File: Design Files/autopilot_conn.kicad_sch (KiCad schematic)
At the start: 7 parts, among them J10 Conn_01x06_MountingPin, J12 Conn_01x02_MountingPin, J13 Conn_01x02_MountingPin, J3 Conn_01x04_MountingPin, J4 Conn_01x06_MountingPin, J6 Conn_01x04_MountingPin, J9 Conn_01x04_MountingPin

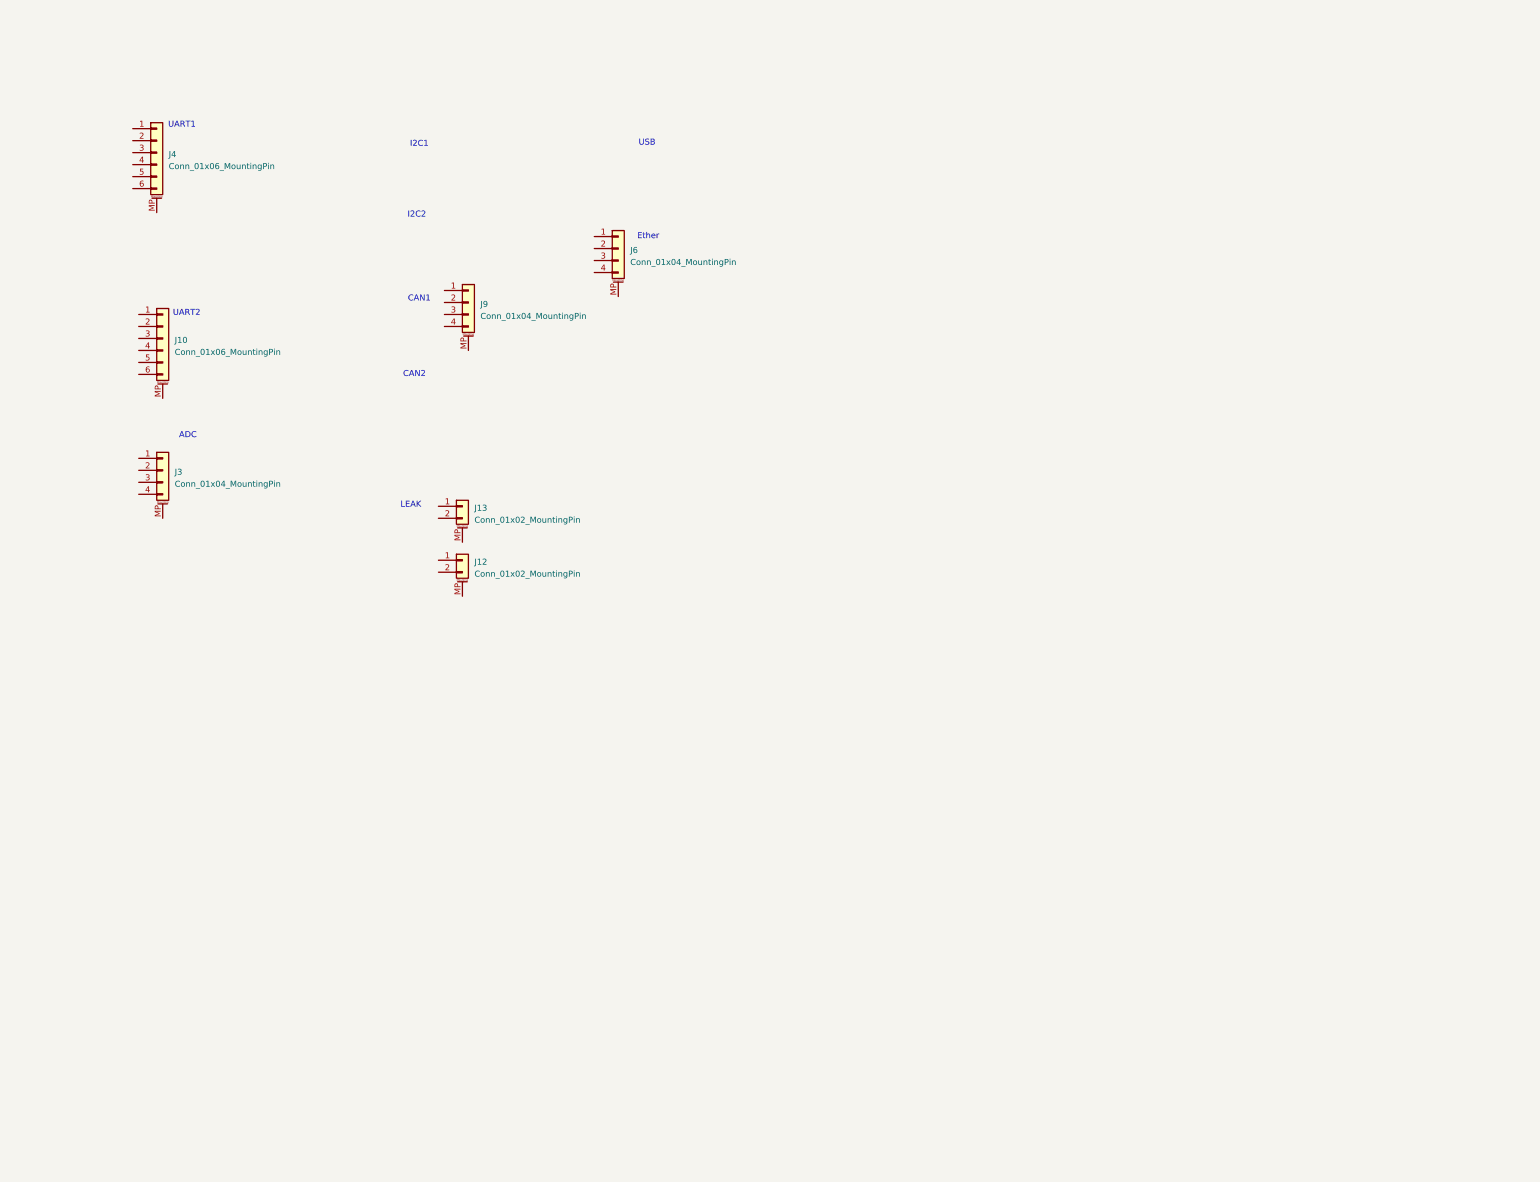
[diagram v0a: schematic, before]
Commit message: More interface interconnects
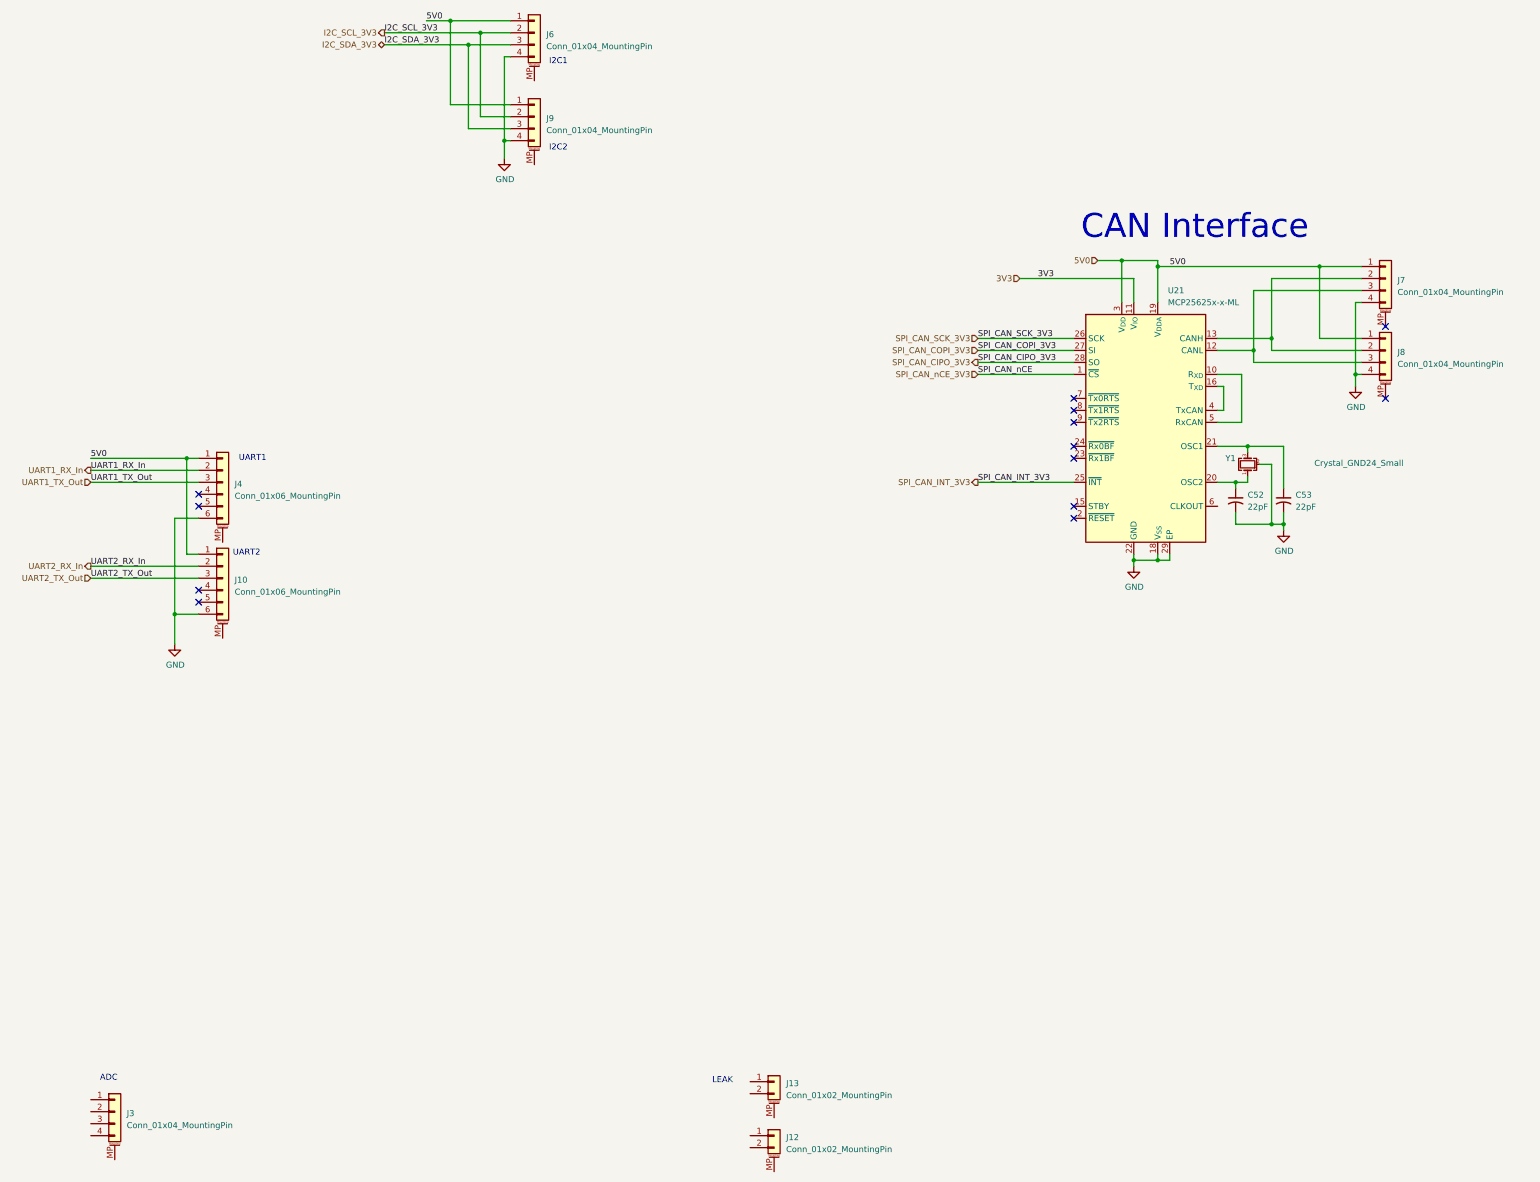
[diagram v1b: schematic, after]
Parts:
- added C52, C53: 22pF, Capacitor_SMD:C_0402_1005Metric, symbol Device:C_Small_US
- added J7, J8: Conn_01x04_MountingPin, Connector_JST:JST_GH_BM04B-GHS-TBT_1x04-1MP_P1.25mm_Vertical, symbol Connector_Generic_MountingPin:Conn_01x04_MountingPin
- added U21: MCP25625x-x-ML, Package_DFN_QFN:QFN-28-1EP_6x6mm_P0.65mm_EP4.25x4.25mm, symbol Interface_CAN_LIN:MCP25625x-x-ML
- added Y1: Crystal_GND24_Small, Crystal:Crystal_SMD_2016-4Pin_2.0x1.6mm, symbol Device:Crystal_GND24_Small
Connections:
- net 5V0: now reaches J4.1 (Pin_1)
- net 5V0: now also J10.1 (Pin_1), J6.1 (Pin_1), J9.1 (Pin_1), J7.1 (Pin_1), J8.1 (Pin_1), U21.19 (V_{DDA}), U21.3 (V_{DD})
- net UART1_RX_In: now reaches J4.2 (Pin_2)
- net UART1_TX_Out: now reaches J4.3 (Pin_3)
- net GND: now reaches J4.6 (Pin_6)
- net GND: now also J10.6 (Pin_6), J6.4 (Pin_4), J9.4 (Pin_4), C52.2, C53.2, J7.4 (Pin_4), J8.4 (Pin_4), U21.18 (V_{SS}), U21.22 (GND), U21.29 (EP), Y1.2 (G), Y1.4 (G)
- net UART2_RX_In: now reaches J10.2 (Pin_2)
- net UART2_TX_Out: now reaches J10.3 (Pin_3)
- net I2C_SCL_3V3: now reaches J6.2 (Pin_2)
- net I2C_SCL_3V3: now also J9.2 (Pin_2)
- net I2C_SDA_3V3: now reaches J6.3 (Pin_3)
- net I2C_SDA_3V3: now also J9.3 (Pin_3)
- new net: J7.2 (Pin_2), J8.2 (Pin_2), U21.13 (CANH)
- new net: J7.3 (Pin_3), J8.3 (Pin_3), U21.12 (CANL)
- new net: U21.10 (R_{XD}), U21.5 (RxCAN)
- new net: U21.16 (T_{XD}), U21.4 (TxCAN)
- new net: C52.1, U21.20 (OSC2), Y1.1
- new net: C53.1, U21.21 (OSC1), Y1.3
- new net 3V3: U21.11 (V_{IO})
- new net SPI_CAN_CIPO_3V3: U21.28 (SO)
- new net SPI_CAN_COPI_3V3: U21.27 (SI)
- new net SPI_CAN_INT_3V3: U21.25 (~{INT})
- new net SPI_CAN_SCK_3V3: U21.26 (SCK)
- new net SPI_CAN_nCE_3V3: U21.1 (~{CS})
- no-connect marks 0 -> 13
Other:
- note added: "CAN Interface"
- note removed: "CAN1"
- note removed: "CAN2"
- note removed: "Ether"
- note removed: "USB"
- moved on the sheet: J10, J12, J13, J3, J4, J6, J9

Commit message: Fixed power & GPIO nets
Added PWM I2C Bus
Replaced global power labels on the sensor page with hierarchical pins & page labels
Cleaned up CM5 GPIO block sheet
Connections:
- net CAN_H: now reaches J7.2 (Pin_2), J8.2 (Pin_2), U21.13 (CANH)
- net CAN_L: now reaches J7.3 (Pin_3), J8.3 (Pin_3), U21.12 (CANL)
- no-connect marks 13 -> 20
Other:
- note added: "I2C Interface"
- note added: "Serial Interface"
- note added: "TODO: 5V Tolerant Buffer for I2C/UART"
- moved on the sheet: C52, C53, J10, J4, J6, J7, J8, J9, U21, Y1

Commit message: Additional layout updates
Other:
- note added: "TODO: ADD CAPACITANCE!!!!"

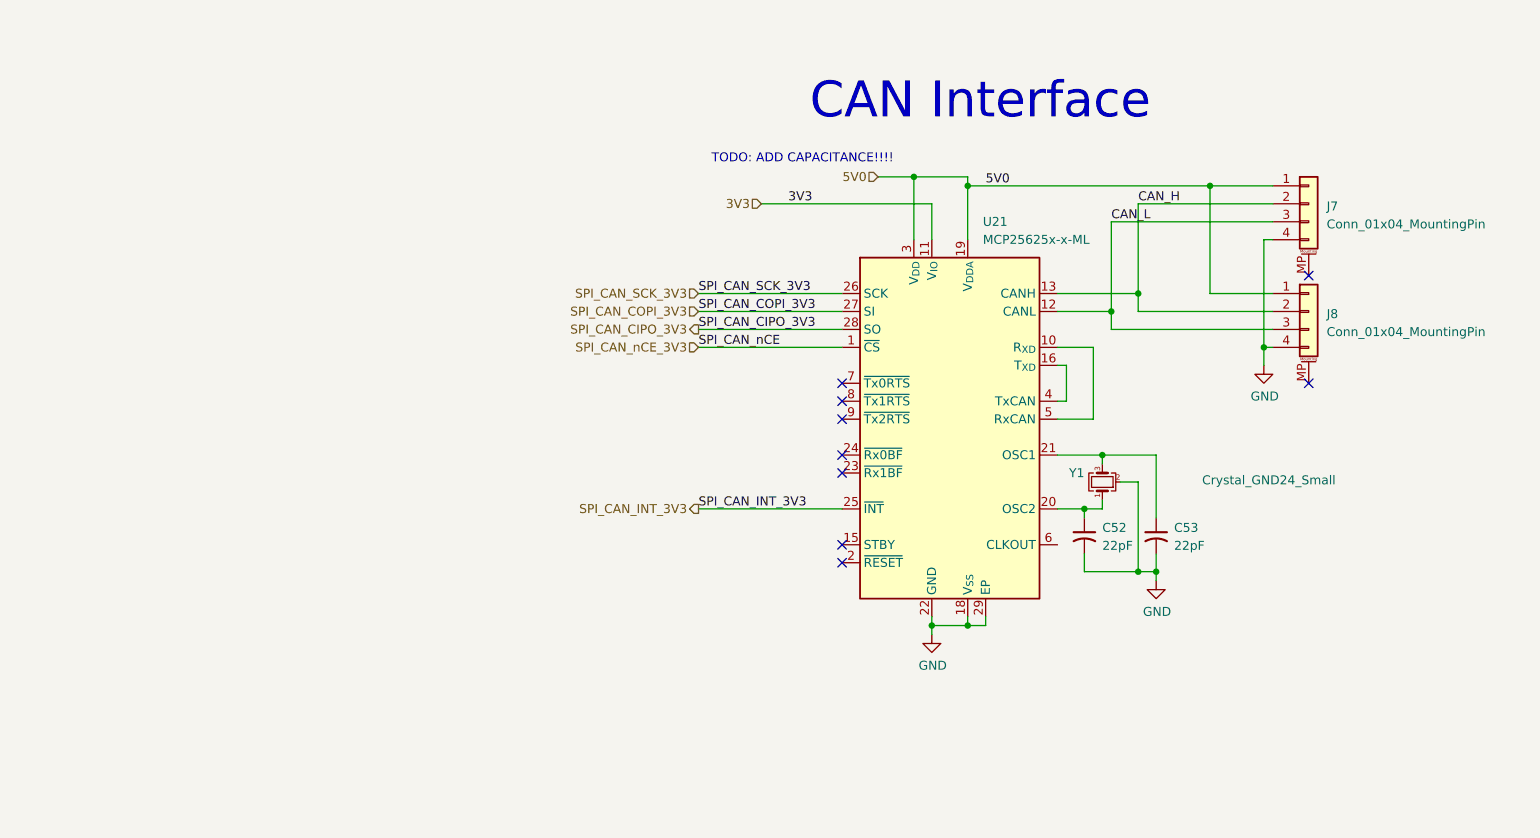
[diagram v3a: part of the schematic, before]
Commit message: Provisional CAN interface design/layout. Probably need to move more north
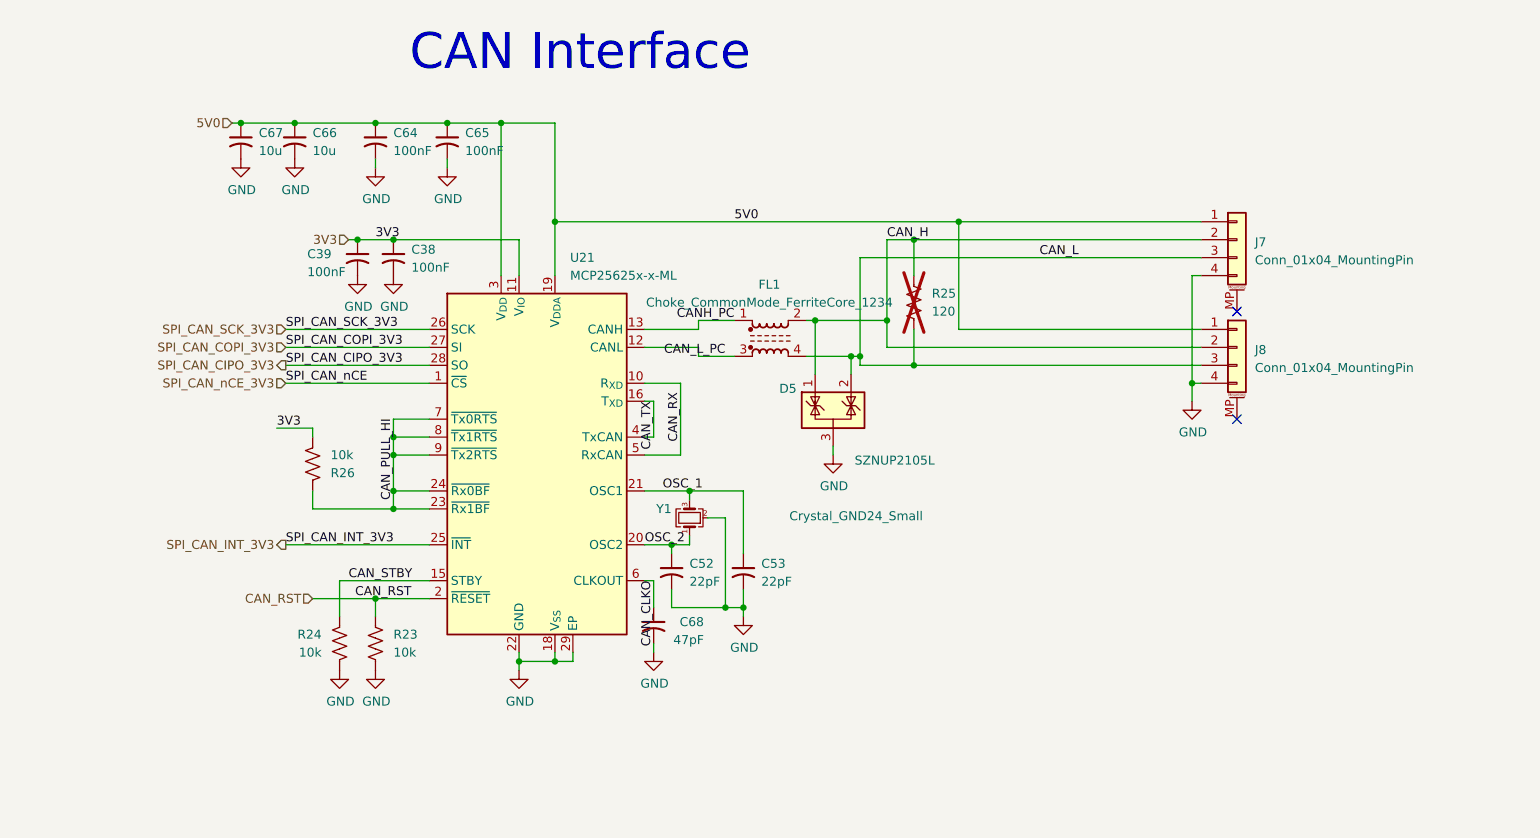
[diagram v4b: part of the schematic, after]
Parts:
- added C38, C39, C64, C65: 100nF, Capacitor_SMD:C_0402_1005Metric, symbol Device:C_Small_US
- added C66, C67: 10u, Capacitor_SMD:C_0201_0603Metric, symbol Device:C_Small_US
- added C68: 47pF, Capacitor_SMD:C_0402_1005Metric, symbol Device:C_Small_US
- added D5: SZNUP2105L, Package_TO_SOT_SMD:SOT-23, symbol Power_Protection:SZNUP2105L
- added FL1: Choke_CommonMode_FerriteCore_1234, Inductor_SMD:L_CommonModeChoke_Coilcraft_0805USB, symbol Filter:Choke_CommonMode_FerriteCore_1234
- added R23, R24, R26: 10k, Resistor_SMD:R_0402_1005Metric_Pad0.72x0.64mm_HandSolder, symbol Device:R_US
- added R25: 120, Resistor_SMD:R_0402_1005Metric_Pad0.72x0.64mm_HandSolder, symbol Device:R_US
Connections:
- net 3V3: now also C38.1, C39.1, R26.2
- net 5V0: now also C64.1, C65.1, C66.1, C67.1
- net CAN_H: now also D5.1 (K), FL1.2, R25.1; no longer U21.13 (CANH)
- net CAN_L: now also D5.2 (K), FL1.4, R25.2; no longer U21.12 (CANL)
- net GND: now also C38.2, C39.2, C64.2, C65.2, C66.2, C67.2, C68.2, D5.3 (A), R23.2, R24.2
- net CAN_RX: now reaches U21.10 (R_{XD}), U21.5 (RxCAN)
- net CAN_STBY: now reaches U21.15 (STBY)
- net CAN_STBY: now also R24.1
- net CAN_TX: now reaches U21.16 (T_{XD}), U21.4 (TxCAN)
- net CAN_RST: now reaches U21.2 (~{RESET})
- net CAN_RST: now also R23.1
- net OSC_2: now reaches C52.1, U21.20 (OSC2), Y1.1
- net OSC_1: now reaches C53.1, U21.21 (OSC1), Y1.3
- net CAN_PULL_HI: now reaches U21.23 (~{Rx1BF})
- net CAN_PULL_HI: now also U21.24 (~{Rx0BF}), U21.7 (~{Tx0RTS}), U21.8 (~{Tx1RTS}), U21.9 (~{Tx2RTS}), R26.1
- net CAN_CLKO: now reaches U21.6 (CLKOUT)
- net CAN_CLKO: now also C68.1
- new net CANH_PC: FL1.1, U21.13 (CANH)
- new net CAN_L_PC: FL1.3, U21.12 (CANL)
- no-connect marks 20 -> 13
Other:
- note removed: "TODO: ADD CAPACITANCE!!!!"
- moved on the sheet: C52, C53, J7, J8, U21, Y1

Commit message: Misc
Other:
- note removed: "TODO: 5V Tolerant Buffer for I2C/UART"
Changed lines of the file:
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@@
-		)
-	)
-	(text "TODO: 5V Tolerant Buffer for I2C/UART"
-		(exclude_from_sim no)
-		(at 156.972 205.486 0)
-		(effects
-			(font
-				(size 5.08 5.08)
-			)
 		)
 	)
